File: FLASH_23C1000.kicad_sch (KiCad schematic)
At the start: 8 parts

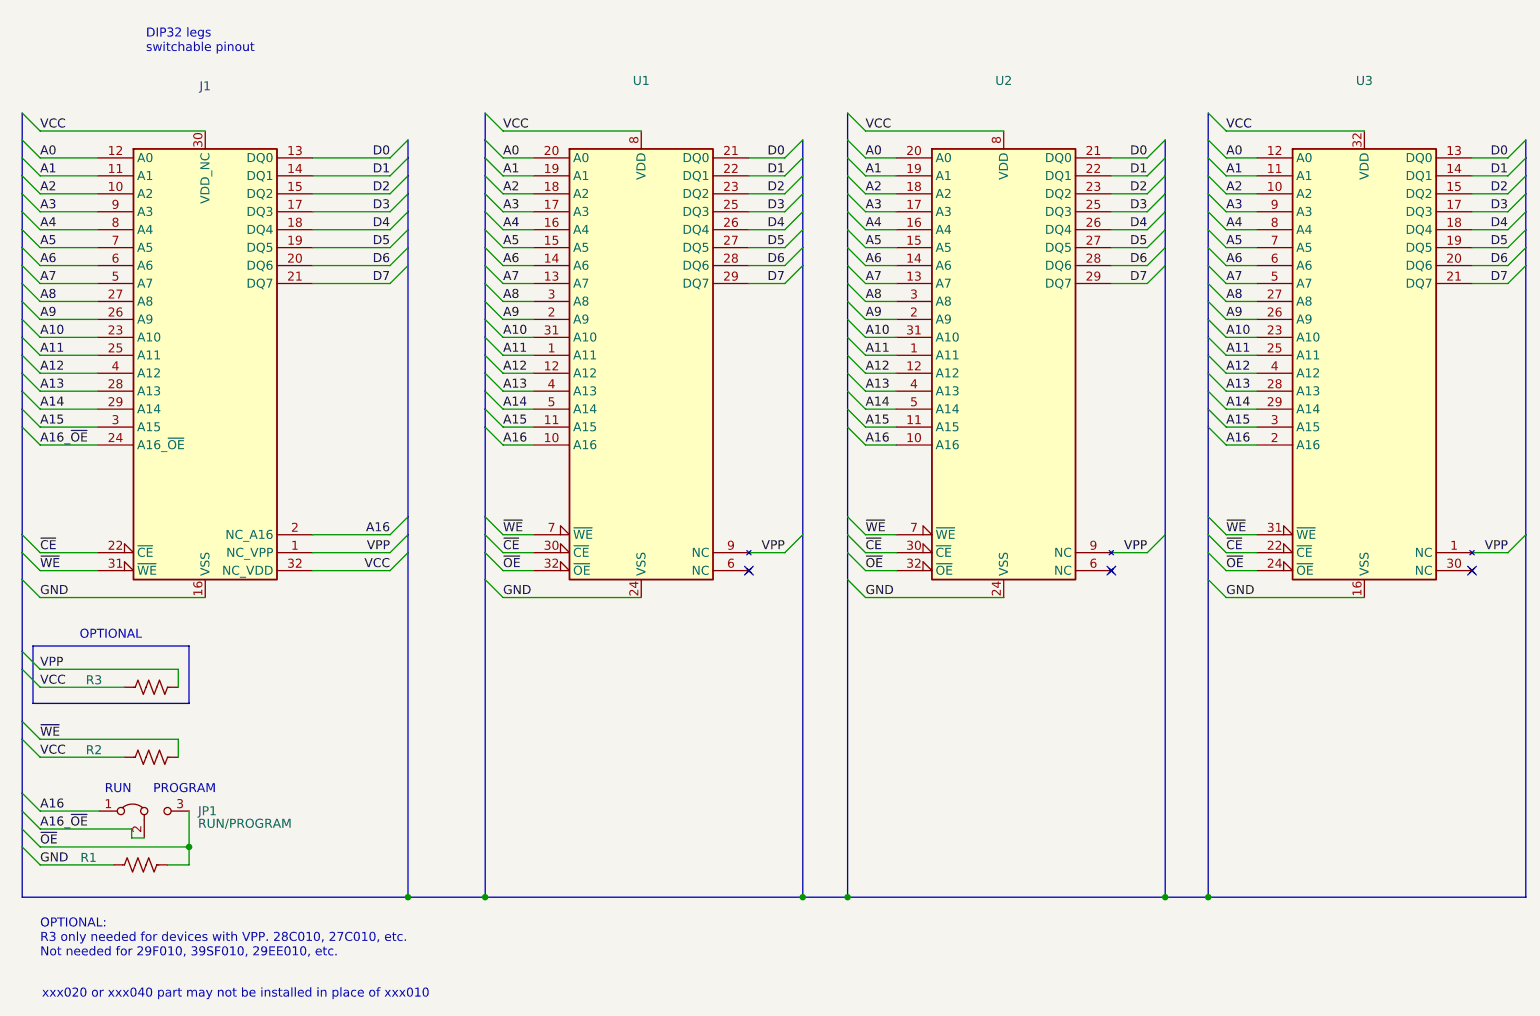
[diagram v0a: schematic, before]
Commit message: 23C1000 silk, sch, gnd
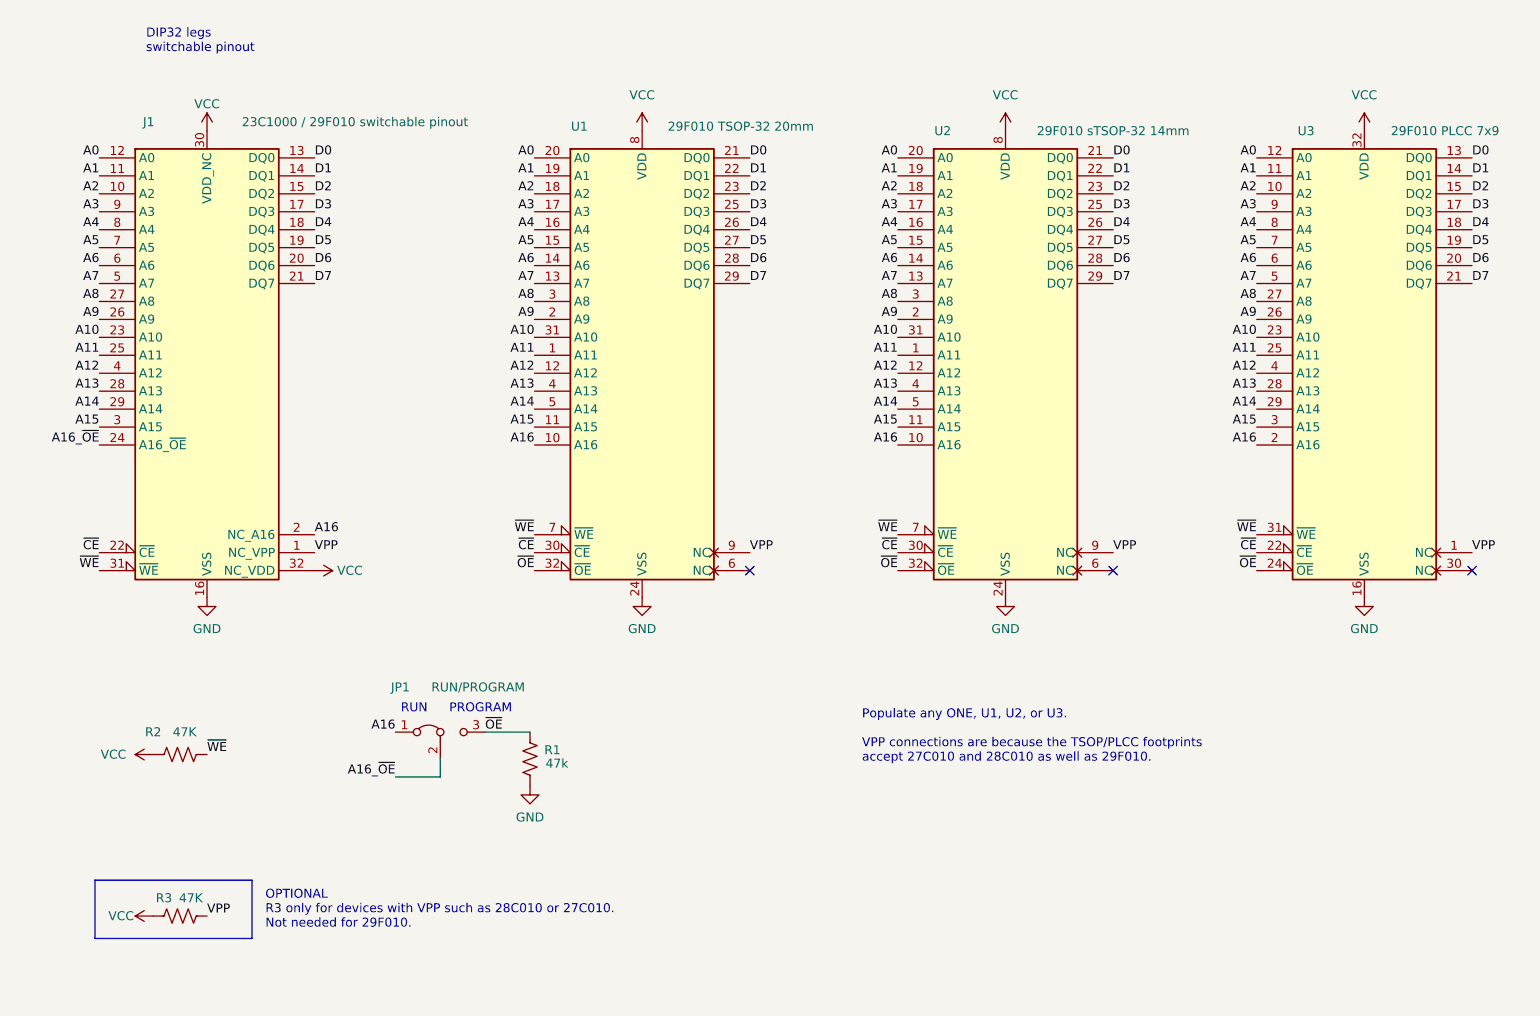
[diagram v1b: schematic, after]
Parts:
- J1: value (none) -> 23C1000 / 29F010 switchable pinout; footprint (none) -> 000_LOCAL:DIP32_DIP28_0.6_pcb_sil_pins
- R1: value (none) -> 47k; footprint (none) -> 000_LOCAL:R_0805
- R2, R3: value (none) -> 47K; footprint (none) -> 000_LOCAL:R_0805
- U1: value (none) -> 29F010 TSOP-32 20mm; footprint (none) -> 000_LOCAL:TSOP32-20mm
- U2: value (none) -> 29F010 sTSOP-32 14mm; footprint (none) -> 000_LOCAL:TSOP32-14mm
- U3: value (none) -> 29F010 PLCC 7x9; footprint (none) -> 000_LOCAL:PLCC32_7x9
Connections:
- net VCC: now also R2.1; no longer R2.2
- net ~{WE}: now also R2.2; no longer R2.1
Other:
- note added: "OPTIONAL R3 only for devices with VPP such as 28C010 or 27C010. Not needed for 29F010."
- note added: "Populate any ONE, U1, U2, or U3. VPP connections are because the TSOP/PLCC footprints accept 27C010 and 28C010 as well as 29F010."
- note removed: "OPTIONAL"
- note removed: "OPTIONAL: R3 only needed for devices with VPP. 28C010, 27C010, etc. Not needed for 29F010, 39SF010, 29EE010, etc."
- note removed: "xxx020 or xxx040 part may not be installed in place of xxx010"
- moved on the sheet: JP1, R1, R2, R3

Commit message: dual-tsop footprint on flash_23c1000
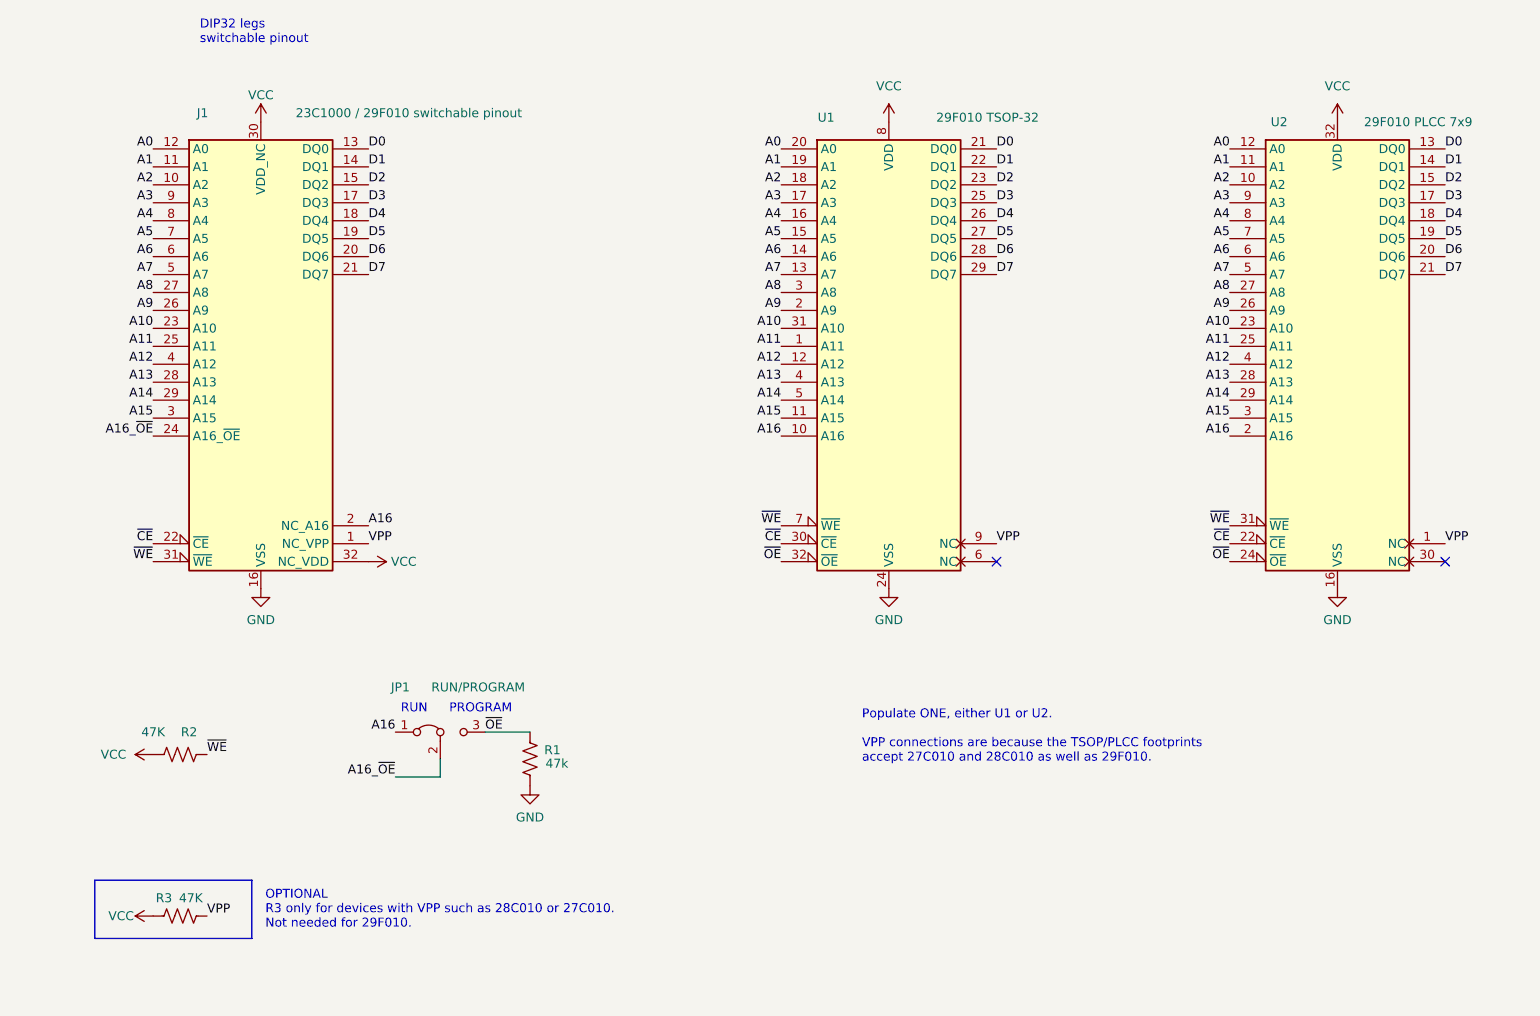
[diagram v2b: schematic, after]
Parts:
- removed U2: 29F010 sTSOP-32 14mm, 000_LOCAL:TSOP32-14mm, symbol 000_LOCAL:SST39SF010_TSOP
- U1: value 29F010 TSOP-32 20mm -> 29F010 TSOP-32; footprint 000_LOCAL:TSOP32-20mm -> 000_LOCAL:TSOP32-dual
- renumbered U3 to U2
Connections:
- net VCC: now also R2.2; no longer R2.1
- net ~{WE}: now also R2.1; no longer R2.2
- no-connect marks 3 -> 2
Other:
- note added: "Populate ONE, either U1 or U2. VPP connections are because the TSOP/PLCC footprints accept 27C010 and 28C010 as well as 29F010."
- note removed: "Populate any ONE, U1, U2, or U3. VPP connections are because the TSOP/PLCC footprints accept 27C010 and 28C010 as well as 29F010."
- moved on the sheet: J1, R2, U1, U2
